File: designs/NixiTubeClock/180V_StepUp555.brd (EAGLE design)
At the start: 160 x 100 mm, 8 parts, among them IC1 LM555D, IC2 IRF740SPBF, T1 BC547

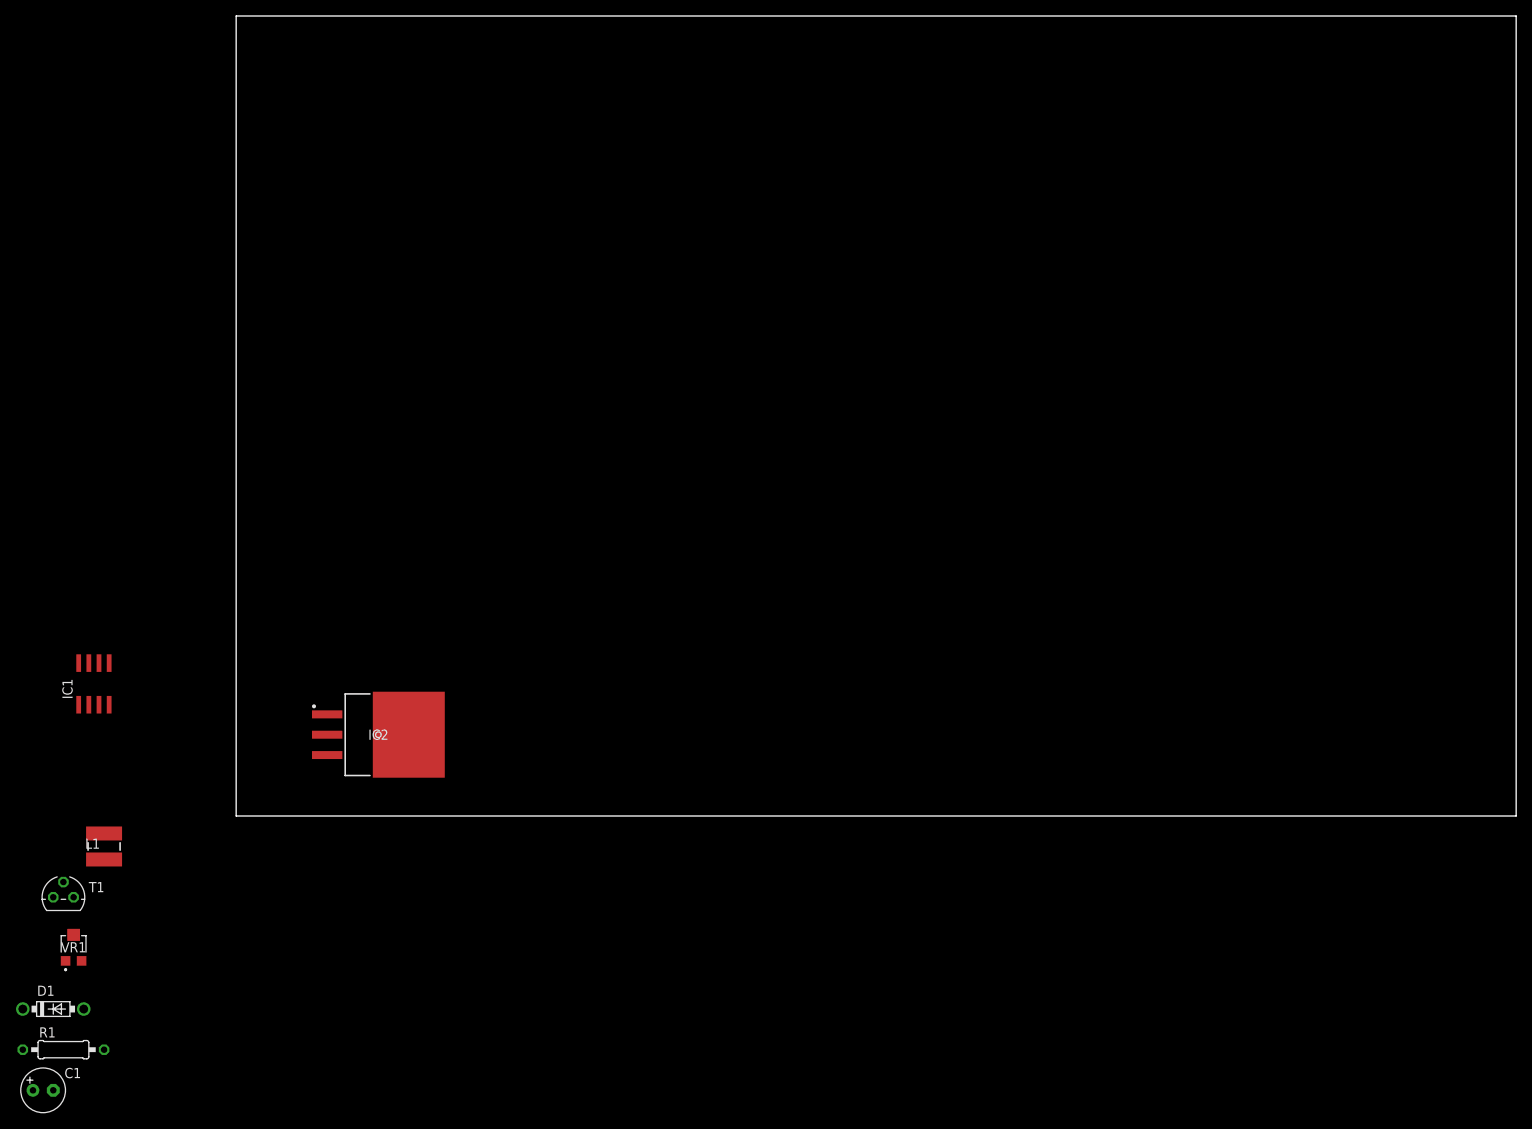
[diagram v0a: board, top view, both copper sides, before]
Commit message: added first IN-4 Design and edited mainboard to fit all screws for IN-4
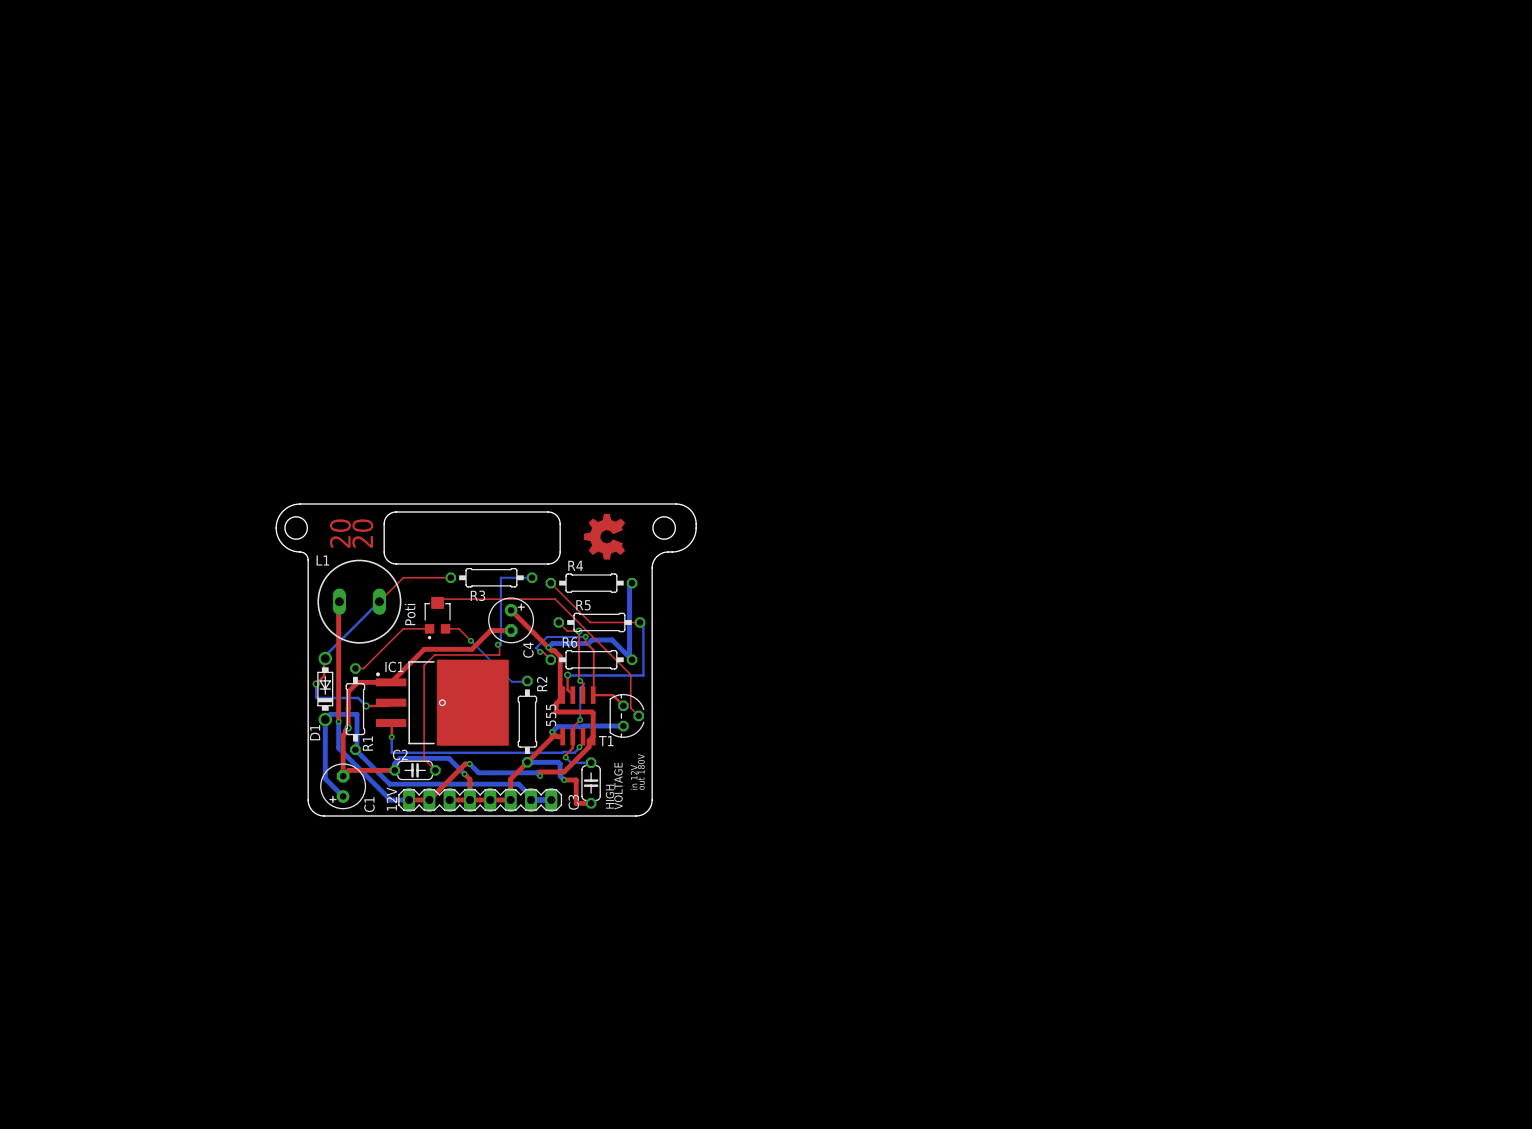
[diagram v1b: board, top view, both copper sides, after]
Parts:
- added C2: 100pF, rcl:C050-024X044
- added C3: 222, rcl:C050-024X044
- added C4: 330uF, rcl:E2,5-6
- added R2: 470R, CommonParts:0207/10
- added R3: 2.2k, CommonParts:0207/10
- added R4: 1k, CommonParts:0207/10
- added R5: 10k, CommonParts:0207/10
- added R6: 56k, CommonParts:0207/10
- added SV2: (no value), con-lstb:MA08-1
- C1: value (none) -> 2.2uF
- D1: value (none) -> UF4004
- IC1: value LM555D -> IRF740SPBF; device linear:SO08 -> CommonParts:TO254P1524X483-4N
- IC2: value IRF740SPBF -> LM555D; device CommonParts:TO254P1524X483-4N -> linear:SO08
- L1: value CD43NP-470KC -> (none); device CommonParts:CD43NP -> inductor-neosid:SD12K100
- R1: value (none) -> 220k
- VR1: value EVM3YSX50B14 -> 1K
- moved T1 73.6 mm to (48.4, 12.5), turned to 270 degrees
- moved VR1 61.6 mm to (25.2, 25.0)
- moved R1 56.1 mm to (14.9, 13.4), turned to 270 degrees
- moved C1 53.4 mm to (13.4, 3.71), turned to 90 degrees
- moved D1 52.5 mm to (11.1, 15.9), turned to 90 degrees
- moved L1 44.2 mm to (15.4, 26.8), turned to 180 degrees
- moved IC1 43.6 mm to (25.8, 14.2)
- moved IC2 25.1 mm to (42.7, 12.5)
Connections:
- removed net V+: IC1.8
- new net +170V: C1.+, D1.C, R1.2, SV2.7, SV2.8
- new net 12V: C4.+, IC2.4, IC2.8, L1.2, R4.2, R6.2, SV2.1, SV2.2
- new net N$1: R2.2, VR1.C1
- new net N$10: IC2.7, R4.1, R5.2
- new net N$12: IC1.3, IC2.3
- new net N$2: R1.1, VR1.A1
- new net N$4: T1.2, VR1.B1
- new net N$5: D1.A, IC1.2, L1.1, R3.2
- new net N$7: IC2.5, R6.1, T1.3
- new net N$8: C2.1, R3.1
- new net N$9: C3.1, IC2.2, IC2.6, R5.1
- net GND: now also C1.-, C2.2, C3.2, C4.-, IC2.1, R2.1, SV2.3, SV2.4, SV2.5, SV2.6, T1.1
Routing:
- net 12V: track 0.00 -> 104.0 mm, vias 0 -> 4
- net GND: track 0.00 -> 97.0 mm, vias 0 -> 4
- net +170V: track 0.00 -> 48.9 mm
- net N$8: track 0.00 -> 37.7 mm, vias 0 -> 1
- net N$5: track 0.00 -> 35.4 mm, vias 0 -> 2
- net N$4: track 0.00 -> 33.8 mm
- net N$10: track 0.00 -> 32.5 mm, vias 0 -> 1
- net N$12: track 0.00 -> 29.1 mm, vias 0 -> 2
- net N$9: track 0.00 -> 25.7 mm, vias 0 -> 4
- net N$7: track 0.00 -> 21.3 mm, vias 0 -> 2
- net N$1: track 0.00 -> 13.0 mm, vias 0 -> 1
- net N$2: track 0.00 -> 11.3 mm
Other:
- board size 160 x 100 mm -> 52.5 x 39 mm
- board text added: "12V"
- board text added: "20 20"
- board text added: "555"
- board text added: "C1"
- board text added: "C2"
- board text added: "D1"
- board text added: "HIGH VOLTAGE"
- board text added: "IC1"
- board text added: "L1"
- board text added: "Poti"
- board text added: "R1"
- board text added: "T1"
- board text added: "in 12V out 180V"

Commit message: worked on brd layout NI-4
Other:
- outline, holes or cut-outs redrawn
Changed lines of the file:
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@@
 <setting verticaltext="up"/>
 </settings>
-<grid distance="0.1" unitdist="mm" unit="mm" style="lines" multiple="1" display="yes" altdistance="5" altunitdist="mm" altunit="mm"/>
+<grid distance="0.5" unitdist="mm" unit="mm" style="lines" multiple="1" display="yes" altdistance="5" altunitdist="mm" altunit="mm"/>
 <layers>
 <layer number="1" name="Top" color="4" fill="1" visible="yes" active="yes"/>
@@
 <wire x1="11" y1="0" x2="50" y2="0" width="0" layer="20"/>
 <wire x1="50" y1="0" x2="52" y2="2" width="0" layer="20" curve="90"/>
-<wire x1="54.5" y1="33" x2="54" y2="33" width="0" layer="20"/>
-<wire x1="54" y1="33" x2="52" y2="31" width="0" layer="20" curve="90"/>
-<wire x1="52" y1="31" x2="52" y2="2" width="0" layer="20"/>
+<wire x1="54.5" y1="33" x2="53" y2="33" width="0" layer="20"/>
+<wire x1="53" y1="33" x2="52" y2="32" width="0" layer="20" curve="90"/>
+<wire x1="52" y1="32" x2="52" y2="2" width="0" layer="20"/>
 <wire x1="40.5" y1="33" x2="40.5" y2="36.5" width="0" layer="20"/>
 <wire x1="40.5" y1="36.5" x2="39" y2="38" width="0" layer="20" curve="90"/>

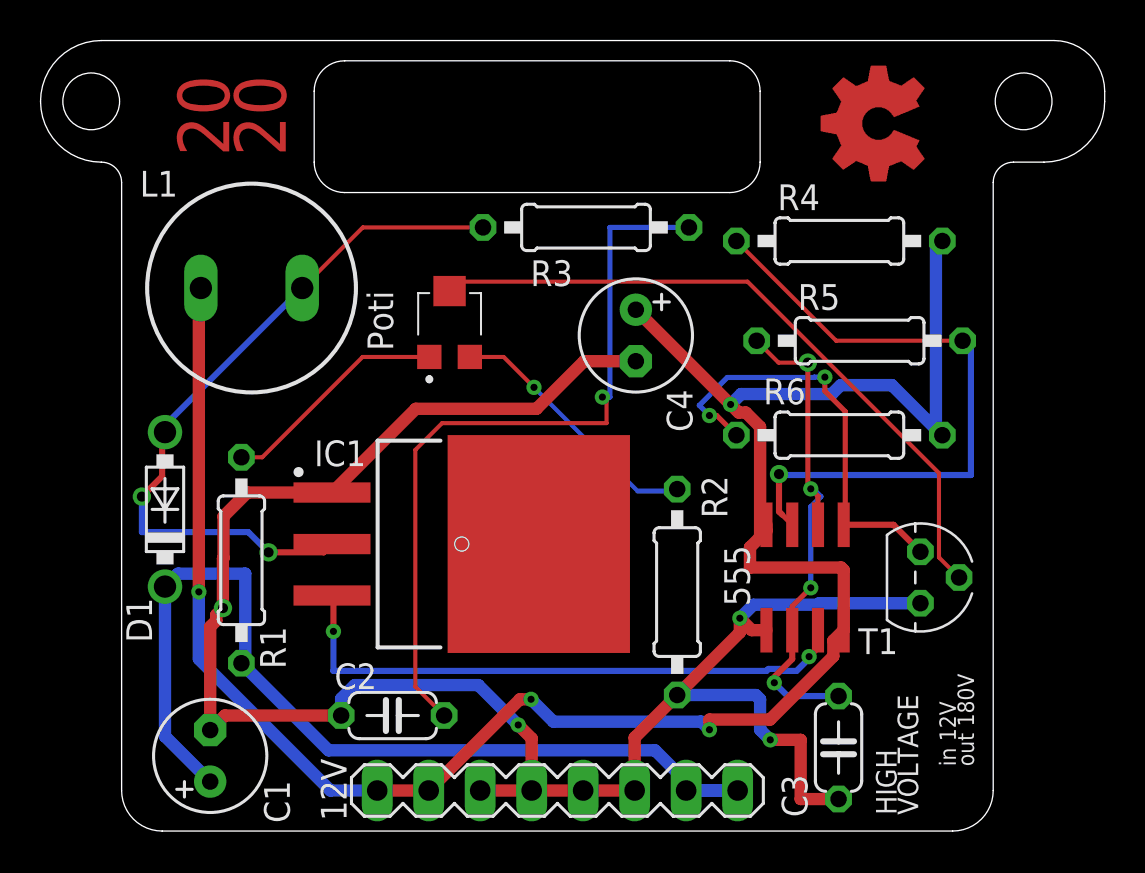
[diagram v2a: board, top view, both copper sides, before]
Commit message: final review of design and ordered from JLC PCB
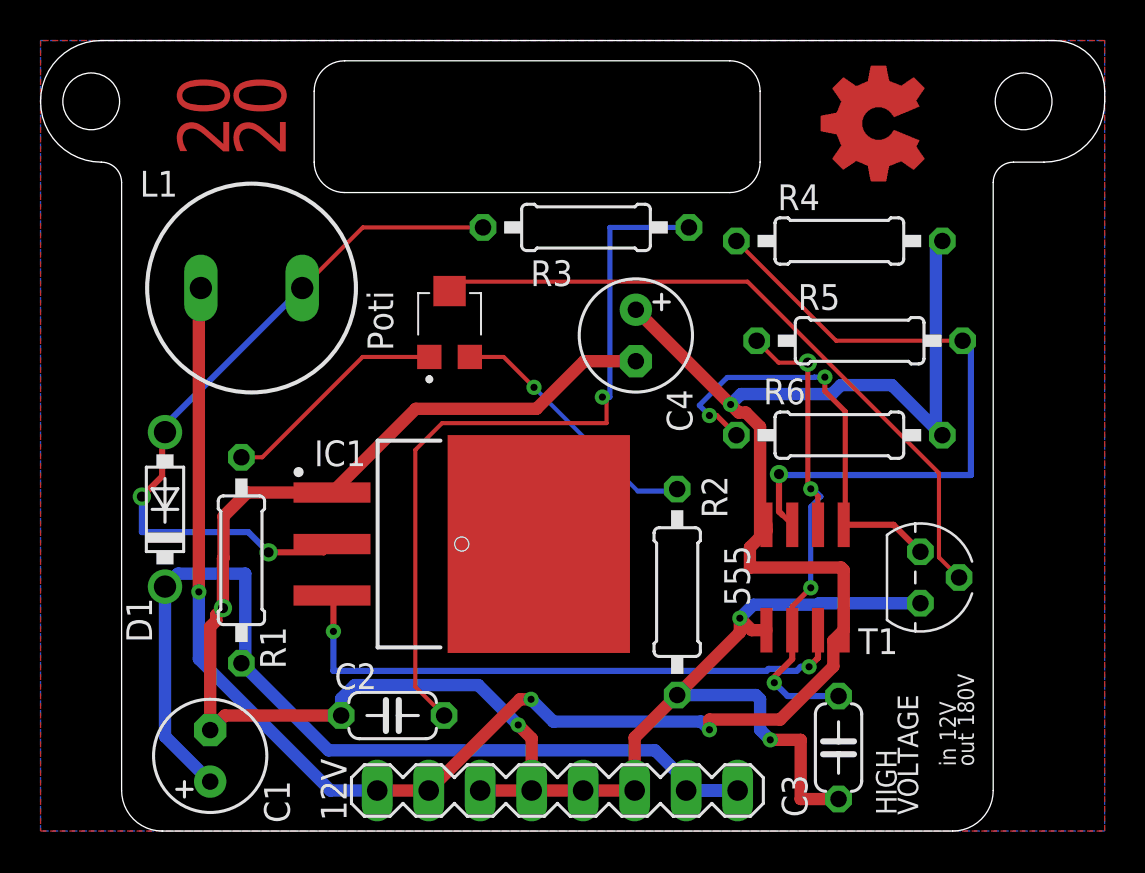
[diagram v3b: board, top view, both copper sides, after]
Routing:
- added copper zone on layer 1, net GND
- added copper zone on layer 16, net GND
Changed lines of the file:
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@@
 <drawing>
 <settings>
-<setting alwaysvectorfont="no"/>
+<setting alwaysvectorfont="yes"/>
 <setting verticaltext="up"/>
 </settings>
@@
 <wire x1="40" y1="14" x2="40.5" y2="14.5" width="0.6096" layer="1"/>
 <wire x1="44.625" y1="9.91" x2="44.1122" y2="9.3972" width="0.6096" layer="1"/>
-<wire x1="44.1122" y1="9.3972" x2="44.1122" y2="8.62061875" width="0.6096" layer="1"/>
-<wire x1="44.1122" y1="8.62061875" x2="40.99158125" y2="5.5" width="0.6096" layer="1"/>
-<wire x1="40.99158125" y1="5.5" x2="38" y2="5.5" width="0.6096" layer="1"/>
+<wire x1="44.1122" y1="9.3972" x2="44.1122" y2="8.12061875" width="0.6096" layer="1"/>
+<wire x1="44.1122" y1="8.12061875" x2="41.49158125" y2="5.5" width="0.6096" layer="1"/>
+<wire x1="41.49158125" y1="5.5" x2="38" y2="5.5" width="0.6096" layer="1"/>
 <wire x1="49.49" y1="19.53" x2="49.47" y2="19.53" width="0.6096" layer="16"/>
 <wire x1="49.47" y1="19.53" x2="47" y2="22" width="0.6096" layer="16"/>
@@
 <contactref element="IC2" pad="3"/>
 <contactref element="IC1" pad="3"/>
-<wire x1="42.9156" y1="8.5156" x2="42.9156" y2="8.60545625" width="0.3048" layer="16"/>
-<via x="42.9156" y="8.60545625" extent="1-16" drill="0.35"/>
-<wire x1="42.9156" y1="8.60545625" x2="43.355" y2="9.04485625" width="0.3048" layer="1"/>
-<wire x1="43.355" y1="9.04485625" x2="43.355" y2="9.91" width="0.3048" layer="1"/>
-<wire x1="42.3" y1="7.9" x2="42.9156" y2="8.5156" width="0.3048" layer="16"/>
+<wire x1="42.50545625" y1="8.10545625" x2="42.9156" y2="8.10545625" width="0.3048" layer="16"/>
+<via x="42.9156" y="8.10545625" extent="1-16" drill="0.35"/>
+<wire x1="42.9156" y1="8.10545625" x2="43.355" y2="8.54485625" width="0.3048" layer="1"/>
+<wire x1="43.355" y1="8.54485625" x2="43.355" y2="9.91" width="0.3048" layer="1"/>
+<wire x1="42.3" y1="7.9" x2="42.50545625" y2="8.10545625" width="0.3048" layer="16"/>
 <via x="19.45" y="9.85" extent="1-16" drill="0.35"/>
 <wire x1="19.38" y1="11.62" x2="19.45" y2="11.55" width="0.3048" layer="1"/>
@@
 <wire x1="13.672" y1="10.38436875" x2="13.672" y2="10.672" width="0.6096" layer="1"/>
 <wire x1="13.672" y1="10.672" x2="14" y2="11" width="0.6096" layer="1"/>
+<polygon width="0.1524" layer="1">
+<vertex x="5" y="39"/>
+<vertex x="5" y="0"/>
+<vertex x="57.5" y="0"/>
+<vertex x="57.5" y="39"/>
+</polygon>
+<polygon width="0.1524" layer="16">
+<vertex x="5" y="39"/>
+<vertex x="57.5" y="39"/>
+<vertex x="57.5" y="0"/>
+<vertex x="5" y="0"/>
+</polygon>
 </signal>
 <signal name="+170V">

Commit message: modified nixi proj. and added EasterRadio project
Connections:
- net GND: now also IC1.3; no longer IC1.1
- net N$12: now also IC1.1; no longer IC1.3
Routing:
- net N$12: track 29.4 -> 38.4 mm
- net GND: track 97.0 -> 102.6 mm
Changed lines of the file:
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@@
 <drawing>
 <settings>
-<setting alwaysvectorfont="yes"/>
+<setting alwaysvectorfont="no"/>
 <setting verticaltext="up"/>
 </settings>
@@
 <signal name="N$12">
 <contactref element="IC2" pad="3"/>
-<contactref element="IC1" pad="3"/>
 <wire x1="42.50545625" y1="8.10545625" x2="42.9156" y2="8.10545625" width="0.3048" layer="16"/>
 <via x="42.9156" y="8.10545625" extent="1-16" drill="0.35"/>
@@
 <wire x1="43.355" y1="8.54485625" x2="43.355" y2="9.91" width="0.3048" layer="1"/>
 <wire x1="42.3" y1="7.9" x2="42.50545625" y2="8.10545625" width="0.3048" layer="16"/>
-<via x="19.45" y="9.85" extent="1-16" drill="0.35"/>
-<wire x1="19.38" y1="11.62" x2="19.45" y2="11.55" width="0.3048" layer="1"/>
-<wire x1="19.45" y1="11.55" x2="19.45" y2="9.85" width="0.3048" layer="1"/>
-<wire x1="19.45" y1="9.85" x2="19.45" y2="7.9" width="0.3048" layer="16"/>
-<wire x1="19.45" y1="7.9" x2="40.8170875" y2="7.9" width="0.3048" layer="16"/>
+<wire x1="40.8170875" y1="7.9" x2="19.45" y2="7.9" width="0.3048" layer="16"/>
 <wire x1="40.8170875" y1="7.9" x2="40.9170875" y2="8" width="0.3048" layer="16"/>
 <wire x1="40.9170875" y1="8" x2="41.4829125" y2="8" width="0.3048" layer="16"/>
 <wire x1="41.4829125" y1="8" x2="41.5829125" y2="7.9" width="0.3048" layer="16"/>
 <wire x1="41.5829125" y1="7.9" x2="42.3" y2="7.9" width="0.3048" layer="16"/>
+<contactref element="IC1" pad="1"/>
+<wire x1="16.5" y1="14.53605625" x2="16.5" y2="16.5" width="0.254" layer="16"/>
+<wire x1="16.9826" y1="14.05345625" x2="16.5" y2="14.53605625" width="0.254" layer="16"/>
+<wire x1="19.45" y1="7.9" x2="16.9826" y2="10.3674" width="0.254" layer="16"/>
+<wire x1="16.9826" y1="10.3674" x2="16.9826" y2="14.05345625" width="0.254" layer="16"/>
+<via x="16.5" y="16.5" extent="1-16" drill="0.35"/>
+<wire x1="16.5" y1="16.5" x2="16.7" y2="16.7" width="0.254" layer="1"/>
+<wire x1="16.7" y1="16.7" x2="19.38" y2="16.7" width="0.254" layer="1"/>
 </signal>
 <signal name="GND">
@@
 <contactref element="R2" pad="1"/>
 <contactref element="T1" pad="1"/>
-<contactref element="IC1" pad="1"/>
 <contactref element="C1" pad="-"/>
 <contactref element="C2" pad="2"/>
@@
 <contactref element="C3" pad="2"/>
 <wire x1="14" y1="13.44946875" x2="14.0276" y2="13.47706875" width="0.6096" layer="1"/>
-<wire x1="14.0276" y1="13.47706875" x2="14.0276" y2="15.5276" width="0.6096" layer="1"/>
-<wire x1="15.2" y1="16.7" x2="19.38" y2="16.7" width="0.6096" layer="1"/>
+<wire x1="14.0276" y1="15.5276" x2="14.0276" y2="13.47706875" width="0.6096" layer="1"/>
 <wire x1="14" y1="11" x2="14" y2="13.44946875" width="0.6096" layer="1"/>
-<wire x1="14.0276" y1="15.5276" x2="15.2" y2="16.7" width="0.6096" layer="1"/>
 <wire x1="31.81658125" y1="23.18" x2="34.37" y2="23.18" width="0.6096" layer="1"/>
-<wire x1="29.46938125" y1="20.8328" x2="31.81658125" y2="23.18" width="0.6096" layer="1"/>
-<wire x1="19.38" y1="16.7" x2="23.5128" y2="20.8328" width="0.6096" layer="1"/>
-<wire x1="23.5128" y1="20.8328" x2="29.46938125" y2="20.8328" width="0.6096" layer="1"/>
+<wire x1="31.81658125" y1="23.18" x2="29.46938125" y2="20.8328" width="0.6096" layer="1"/>
 <via x="14" y="11" extent="1-16" drill="0.5"/>
 <wire x1="44.37" y1="1.58" x2="42.5" y2="1.58" width="0.6096" layer="1"/>
@@
 <vertex x="5" y="0"/>
 </polygon>
+<contactref element="IC1" pad="3"/>
+<wire x1="14" y1="11" x2="16.5" y2="11" width="0.6096" layer="1"/>
+<wire x1="17.12" y1="11.62" x2="17.5" y2="11.62" width="0.6096" layer="1"/>
+<wire x1="17.5" y1="11.62" x2="18.65789375" y2="11.62" width="0.6096" layer="1"/>
+<wire x1="16.5" y1="11" x2="17.12" y2="11.62" width="0.6096" layer="1"/>
+<wire x1="29.46938125" y1="20.8328" x2="19.3328" y2="20.8328" width="0.6096" layer="1"/>
+<wire x1="19.3328" y1="20.8328" x2="14.0276" y2="15.5276" width="0.6096" layer="1"/>
+<wire x1="18.65789375" y1="11.62" x2="19.38" y2="11.62" width="0.6096" layer="1"/>
 </signal>
 <signal name="+170V">
